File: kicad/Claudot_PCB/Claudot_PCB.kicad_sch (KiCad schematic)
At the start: 63 parts, among them J1 TYPE-C-31-M-12, J2 Conn_01x12, SW1 SW_Push, SW10 SW_Push, SW11 SW_Push, SW12 RotaryEncoder, SW2 SW_Push, SW3 SW_Push, SW4 SW_Push, SW5 SW_Push, SW6 SW_Push, SW7 SW_Push, SW8 SW_Push, SW9 SW_Push, U1 RP2040, U2 W25Q16JVUXIQ, U3 AP2112K-3.3, Y1 12MHz

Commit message: Update schematic and pcb
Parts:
- added J3: Conn_01x12, Library:AFC01-S12FCC-00, symbol Connector_Generic:Conn_01x12
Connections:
- net +3V3: now also J2.1 (Pin_1), J3.1 (Pin_1)
- net GND: now also J2.12 (Pin_12), J3.12 (Pin_12)
- net ROW1: now reaches SW7.1
- net ROW1: now also SW11.1, SW2.1, J3.3 (Pin_3)
- net COL0: now reaches D4.1 (K)
- net COL0: now also D1.1 (K), D2.1 (K), D3.1 (K), D5.1 (K), J3.7 (Pin_7)
- net ROW0: now reaches SW6.1
- net ROW0: now also SW1.1, SW10.1, J3.2 (Pin_2)
- net ROW3: now reaches SW4.1
- net ROW3: now also SW9.1, J3.5 (Pin_5)
- net ROW4: now reaches SW5.1
- net ROW4: now also J3.6 (Pin_6)
- net at U1.29 (GPIO18): now also J2.2 (Pin_2); no longer J2.1 (Pin_1)
- net at J2.10 (Pin_10): now also U1.38 (GPIO26_ADC0); no longer U1.39 (GPIO27_ADC1)
- net at J2.11 (Pin_11): now also U1.39 (GPIO27_ADC1); no longer U1.40 (GPIO28_ADC2)
- net at U1.41 (GPIO29_ADC3): no longer J2.12 (Pin_12)
- net at U1.30 (GPIO19): now also J2.3 (Pin_3); no longer J2.2 (Pin_2)
- net at U1.31 (GPIO20): now also J2.4 (Pin_4); no longer J2.3 (Pin_3)
- net at U1.32 (GPIO21): now also J2.5 (Pin_5); no longer J2.4 (Pin_4)
- net at U1.34 (GPIO22): now also J2.6 (Pin_6); no longer J2.5 (Pin_5)
- net at U1.35 (GPIO23): now also J2.7 (Pin_7); no longer J2.6 (Pin_6)
- net at U1.36 (GPIO24): now also J2.8 (Pin_8); no longer J2.7 (Pin_7)
- net at U1.37 (GPIO25): now also J2.9 (Pin_9); no longer J2.8 (Pin_8)
- net COL1: now reaches D7.1 (K)
- net COL1: now also D6.1 (K), D8.1 (K), D9.1 (K), J3.8 (Pin_8)
- net COL2: now reaches D11.1 (K)
- net COL2: now also D10.1 (K), J3.9 (Pin_9)
- net ROW2: now reaches SW8.1
- net ROW2: now also SW3.1, J3.4 (Pin_4)
- net IN-A renamed ROT1A
- net ROT1A: now also J3.10 (Pin_10)
- net IN-B renamed ROT1B
- net ROT1B: now also J3.11 (Pin_11)
- net SW12-A renamed SW12_A
- net SW12-B renamed SW12_B
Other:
- moved on the sheet: J2

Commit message: Update schematic and pcb
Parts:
- SW12: footprint Rotary_Encoder:RotaryEncoder_Alps_EC12E_Vertical_H20mm -> Library:EC12E
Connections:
- net +3V3: now also J3.12 (Pin_12); no longer J3.1 (Pin_1)
- net COL0: now also J3.6 (Pin_6); no longer J3.7 (Pin_7)
- net COL1: now also J3.5 (Pin_5); no longer J3.8 (Pin_8)
- net COL2: now also J3.4 (Pin_4); no longer J3.9 (Pin_9)
- net GND: now also J3.1 (Pin_1); no longer J3.12 (Pin_12)
- net ROT1A: now also J3.3 (Pin_3); no longer J3.10 (Pin_10)
- net ROT1B: now also J3.2 (Pin_2); no longer J3.11 (Pin_11)
- net ROW0: now also J3.11 (Pin_11); no longer J3.2 (Pin_2)
- net ROW1: now also J3.10 (Pin_10); no longer J3.3 (Pin_3)
- net ROW2: now also J3.9 (Pin_9); no longer J3.4 (Pin_4)
- net ROW3: now also J3.8 (Pin_8); no longer J3.5 (Pin_5)
- net ROW4: now also J3.7 (Pin_7); no longer J3.6 (Pin_6)
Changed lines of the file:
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@@
 	(symbol
 		(lib_id "Connector_Generic:Conn_01x12")
-		(at 104.14 96.52 0)
+		(at 104.14 99.06 0)
+		(mirror x)
 		(unit 1)
 		(exclude_from_sim no)
@@
 		(on_board yes)
 		(dnp no)
-		(fields_autoplaced yes)
 		(property "Reference" "J3"
 			(at 106.68 96.5199 0)
@@
 		)
 		(property "Footprint" "Library:AFC01-S12FCC-00"
-			(at 104.14 96.52 0)
+			(at 104.14 99.06 0)
 			(effects
 				(font
@@
 		)
 		(property "Datasheet" "~"
-			(at 104.14 96.52 0)
+			(at 104.14 99.06 0)
 			(effects
 				(font
@@
 		)
 		(property "Description" "Generic connector, single row, 01x12, script generated (kicad-library-utils/schlib/autogen/connector/)"
-			(at 104.14 96.52 0)
+			(at 104.14 99.06 0)
 			(effects
 				(font
@@
 			)
 		)
-		(property "Footprint" "Rotary_Encoder:RotaryEncoder_Alps_EC12E_Vertical_H20mm"
+		(property "Footprint" "Library:EC12E"
 			(at 104.14 58.166 0)
 			(effects

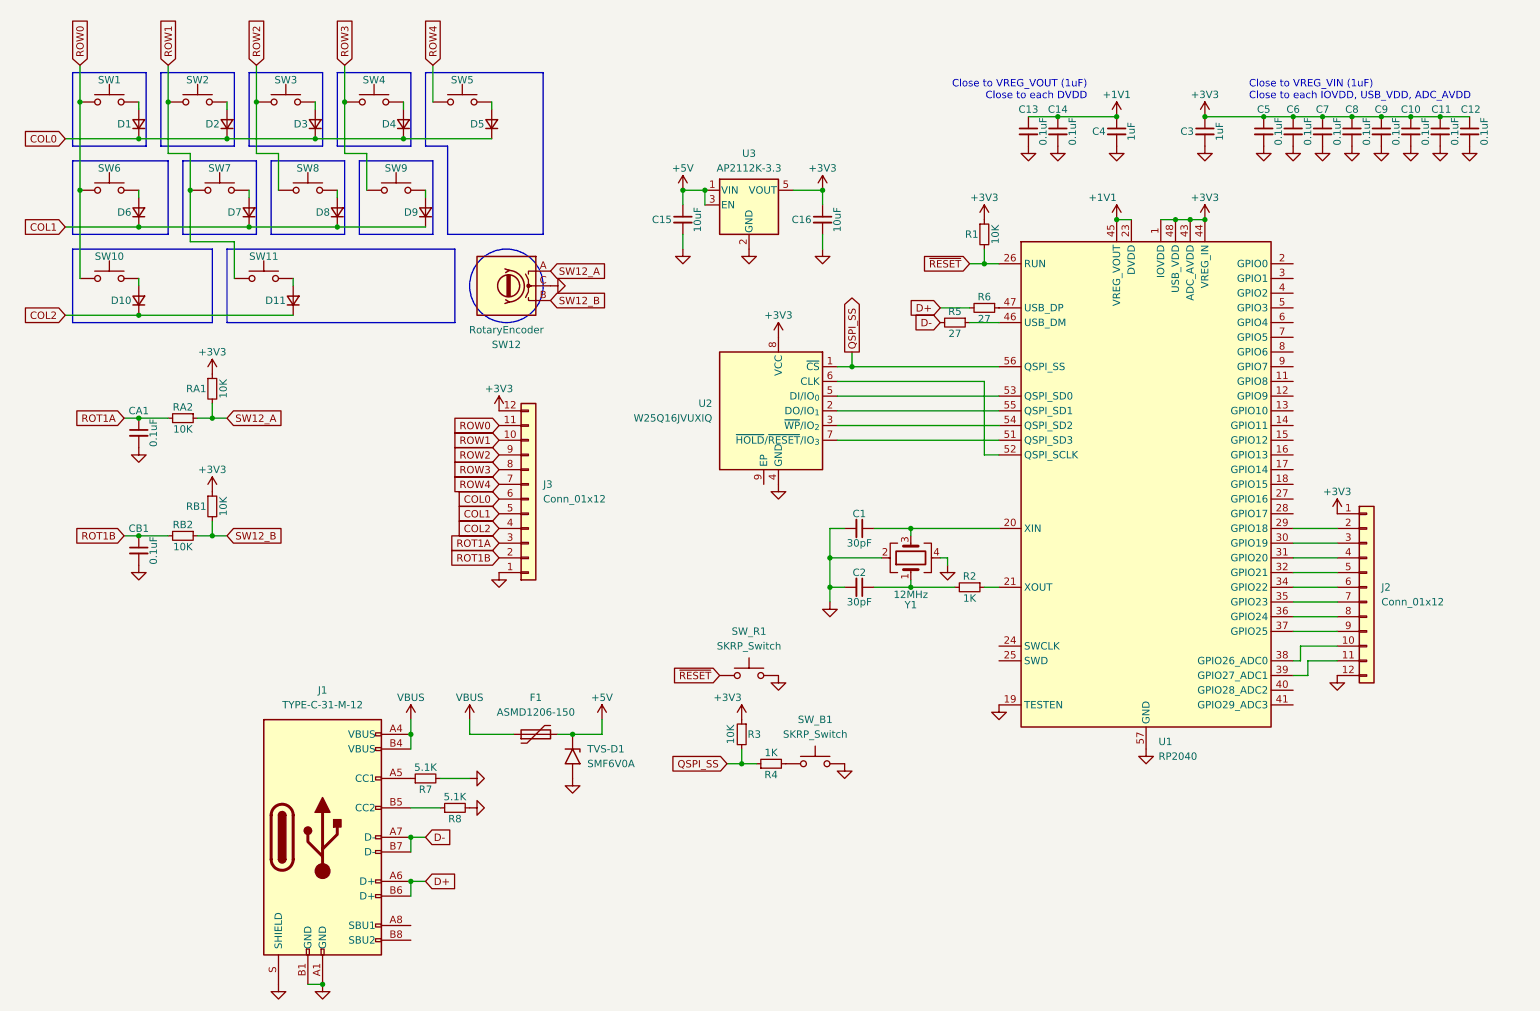
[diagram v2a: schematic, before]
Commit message: Separate PCB designs into individual KiCad projects
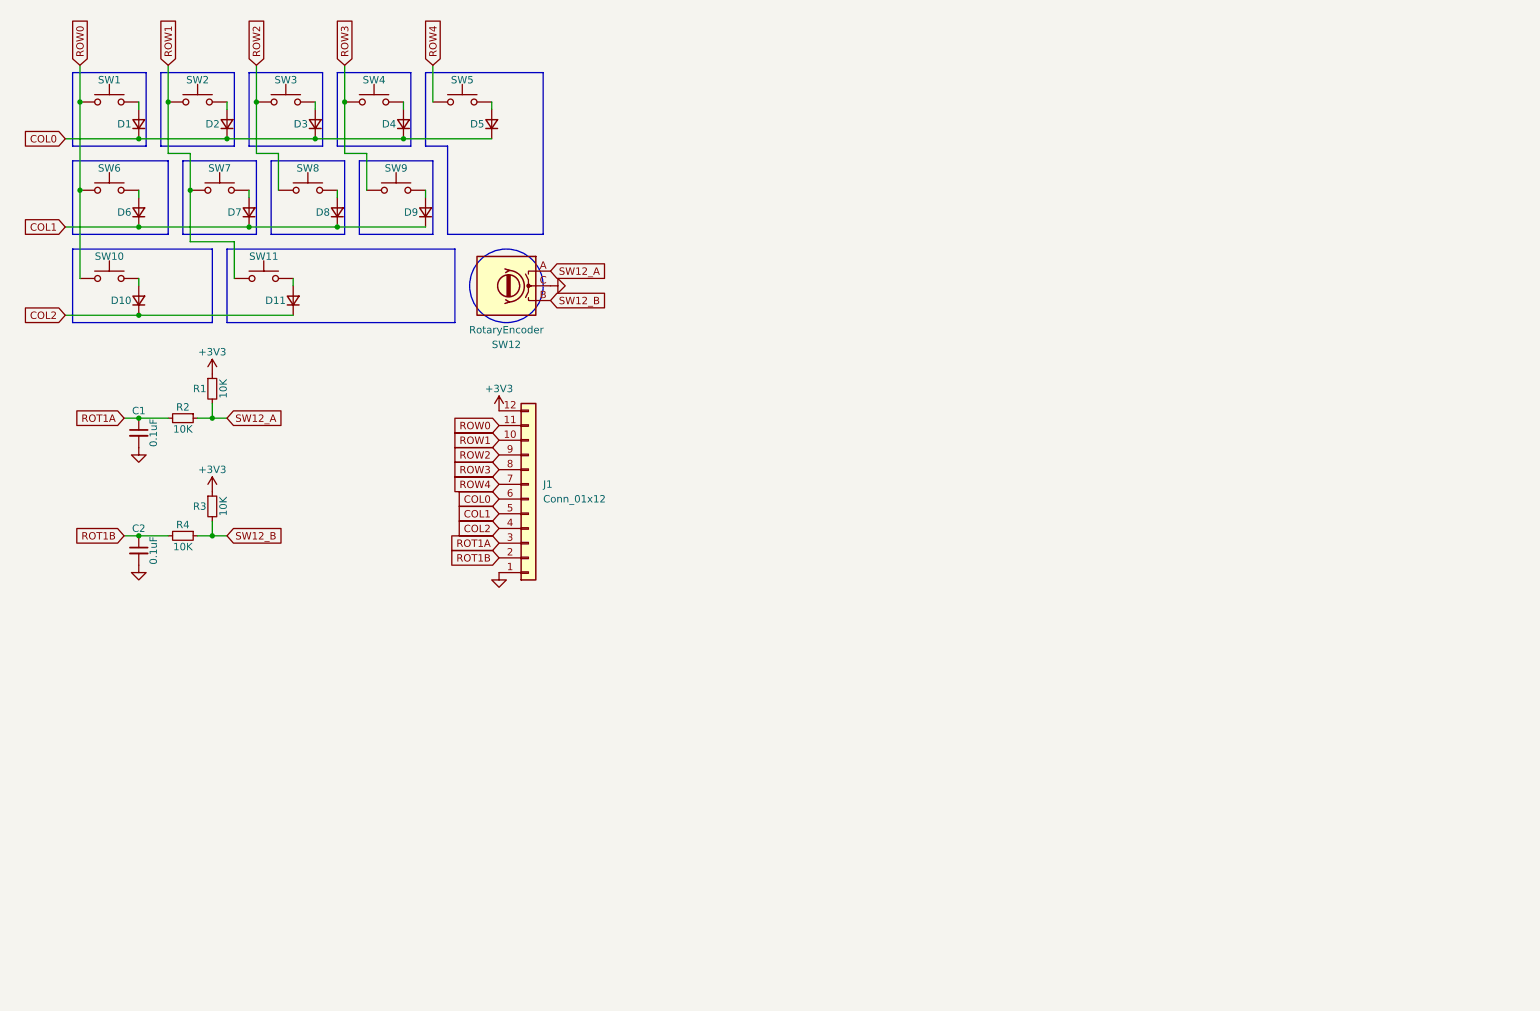
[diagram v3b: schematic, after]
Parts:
- removed C1, C2: 30pF, Library:C_0402, symbol Device:C_Small
- removed C10, C11, C12, C13, C14, C5, C6, C7, C8, C9: 0.1uF, Library:C_0402, symbol Device:C_Small
- removed C15, C16: 10uF, Library:C_0402, symbol Device:C_Small
- removed C3, C4: 1uF, Library:C_0402, symbol Device:C_Small
- removed F1: ASMD1206-150, Library:F_1206, symbol Device:Polyfuse
- removed J1: TYPE-C-31-M-12, Library:TYPE-C-31-M-12, symbol Library:TYPE-C-31-M-12
- removed J2: Conn_01x12, Library:AFC01-S12FCC-00, symbol Connector_Generic:Conn_01x12
- removed R1, R3: 10K, Library:R_0402, symbol Device:R_Small
- removed R2, R4: 1K, Library:R_0402, symbol Device:R_Small
- removed R5, R6: 27, Library:R_0402, symbol Device:R_Small
- removed R7, R8: 5.1K, Library:R_0402, symbol Device:R_Small
- removed SW_B1, SW_R1: SKRP_Switch, Library:SKRP_Switch, symbol Library:SKRP_Switch
- removed TVS-D1: SMF6V0A, Library:SMF6.0A, symbol Diode:SMF6V0A
- removed U1: RP2040, Library:RP2040, symbol MCU_RaspberryPi:RP2040
- removed U2: W25Q16JVUXIQ, Library:W25Q16JVUXIQ, symbol Library:W25Q16JVUXIQ
- removed U3: AP2112K-3.3, Library:SOT25, symbol Regulator_Linear:AP2112K-3.3
- removed Y1: 12MHz, Library:SMD3225-4P, symbol Device:Crystal_GND24
- renumbered CA1 to C1, CB1 to C2, J3 to J1, RA1 to R1, RA2 to R2, RB1 to R3, RB2 to R4
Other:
- note removed: "Close to VREG_VIN (1uF) Close to each IOVDD, USB_VDD, ADC_AVDD"
- note removed: "Close to VREG_VOUT (1uF) Close to each DVDD"

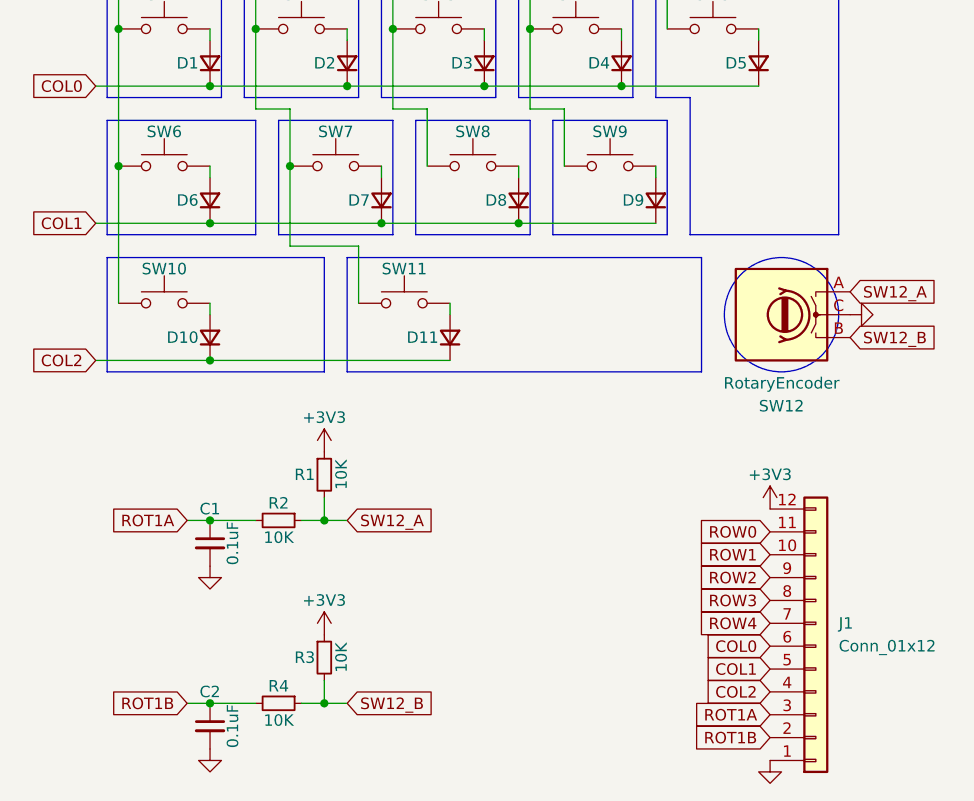
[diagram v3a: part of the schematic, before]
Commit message: kicad: replace rotary encoder with key
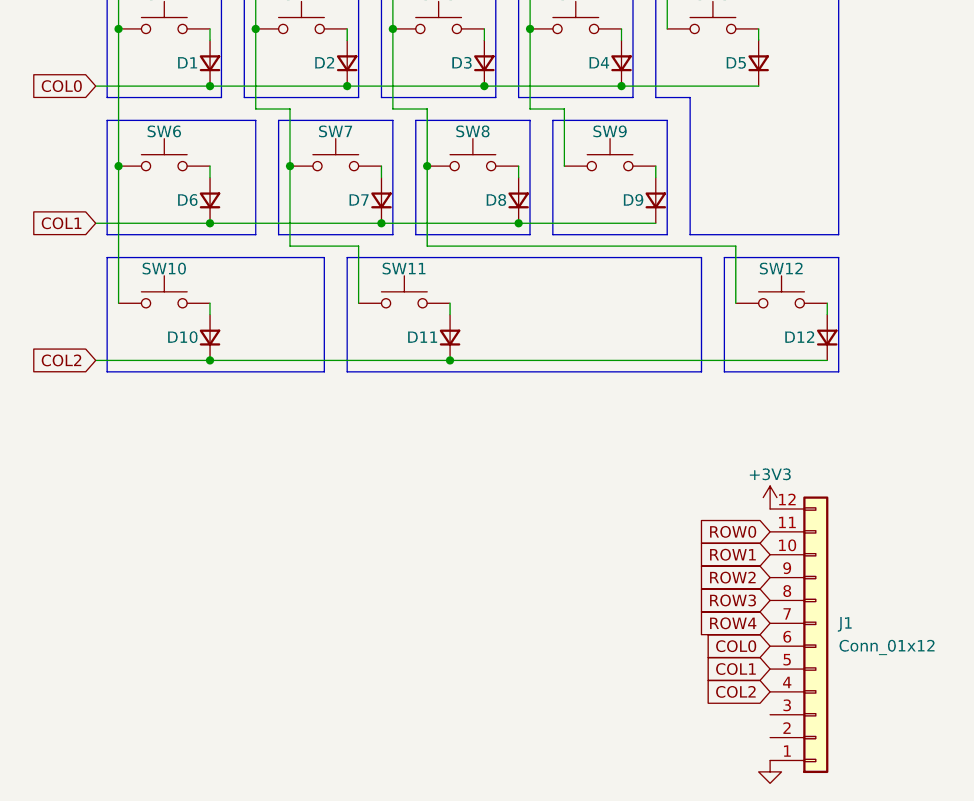
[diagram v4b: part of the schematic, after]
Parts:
- removed C1, C2: 0.1uF, Library:C_0402, symbol Device:C_Small
- removed R1, R2, R3, R4: 10K, Library:R_0402, symbol Device:R_Small
- removed SW12: RotaryEncoder, Library:EC12E, symbol Device:RotaryEncoder
- added D12: D_Small, Library:SOD323, symbol Device:D_Small
- added SW12: SW_Push, Library:CPG151101S11-16, symbol Switch:SW_Push
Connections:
- net COL2: now also D12.1 (K)
- net ROW2: now also SW12.1
- net ROT1A: no longer names the net of J1.3 (Pin_3)
- net ROT1B: no longer names the net of J1.2 (Pin_2)
- new net: D12.2 (A), SW12.2

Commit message: WIP
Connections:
- net +3V3: now also J1.2 (Pin_2); no longer J1.12 (Pin_12)
- net GND: now also J1.12 (Pin_12)

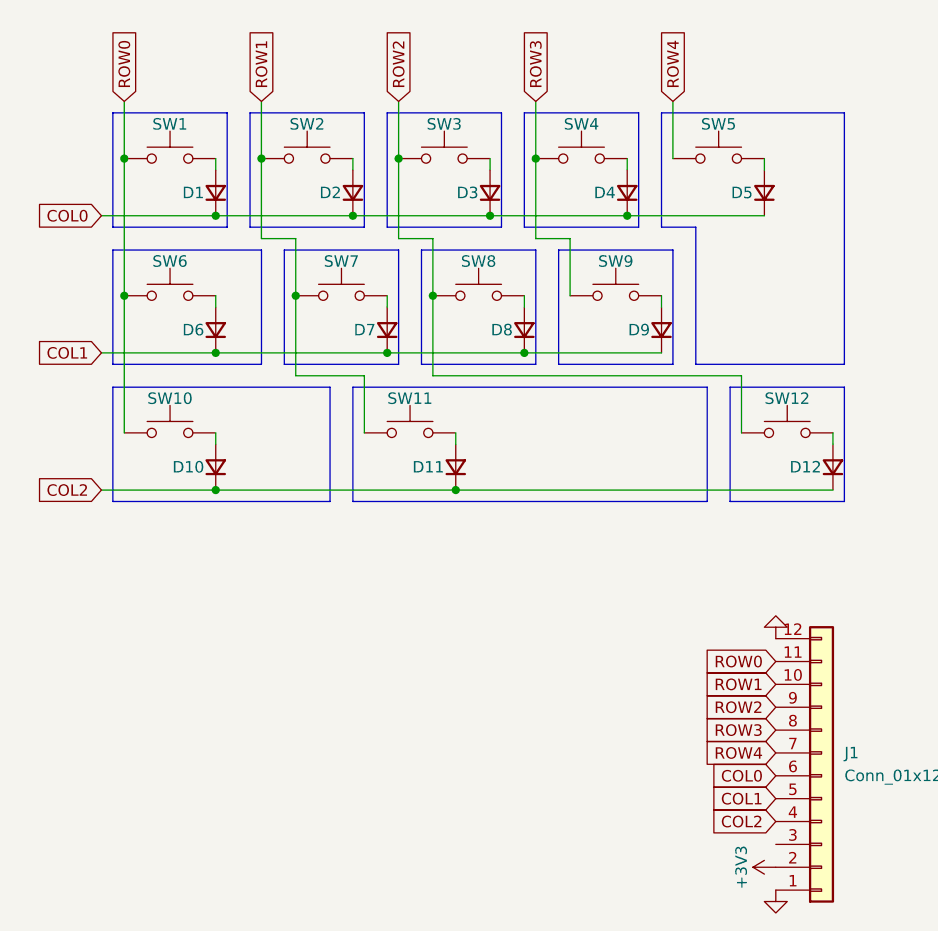
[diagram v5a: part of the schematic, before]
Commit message: fix: correct row/column net labels
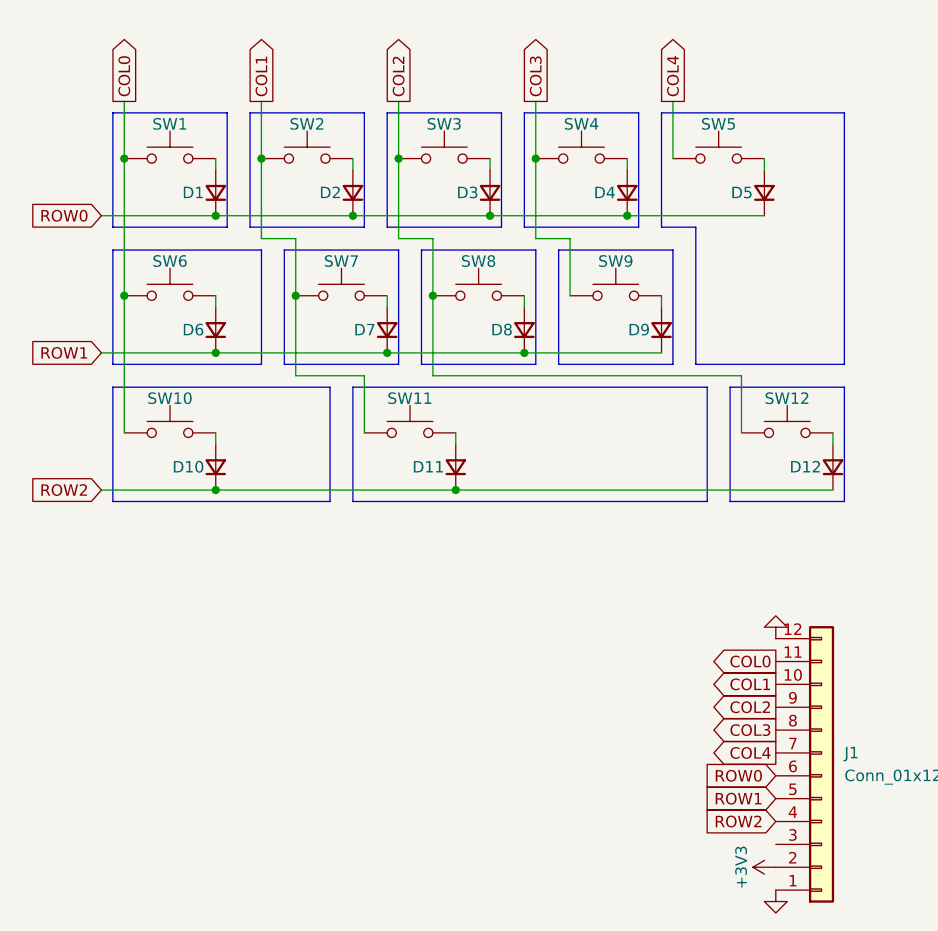
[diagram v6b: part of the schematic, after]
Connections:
- net COL0: now also J1.11 (Pin_11), SW1.1, SW10.1, SW6.1; no longer D1.1 (K), D2.1 (K), D3.1 (K), D4.1 (K), D5.1 (K), J1.6 (Pin_6)
- net COL1: now also J1.10 (Pin_10), SW11.1, SW2.1, SW7.1; no longer D6.1 (K), D7.1 (K), D8.1 (K), D9.1 (K), J1.5 (Pin_5)
- net COL2: now also J1.9 (Pin_9), SW12.1, SW3.1, SW8.1; no longer D10.1 (K), D11.1 (K), D12.1 (K), J1.4 (Pin_4)
- net ROW0: now also D1.1 (K), D2.1 (K), D3.1 (K), D4.1 (K), D5.1 (K), J1.6 (Pin_6); no longer J1.11 (Pin_11), SW1.1, SW10.1, SW6.1
- net ROW1: now also D6.1 (K), D7.1 (K), D8.1 (K), D9.1 (K), J1.5 (Pin_5); no longer J1.10 (Pin_10), SW11.1, SW2.1, SW7.1
- net ROW2: now also D10.1 (K), D11.1 (K), D12.1 (K), J1.4 (Pin_4); no longer J1.9 (Pin_9), SW12.1, SW3.1, SW8.1
- net ROW3 renamed COL3
- net ROW4 renamed COL4

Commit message: feat: finalize Claudot_PCB
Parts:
- removed J1: Conn_01x12, Library:AFC01-S12FCC-00, symbol Connector_Generic:Conn_01x12
- added J1: Conn_01x08, Library:AFC01-S08FCC-00, symbol Connector_Generic:Conn_01x08
- renumbered D11 to D10, D12 to D11, D5 to D12, D6 to D5, D7 to D6, D8 to D7, D9 to D8, D10 to D9, SW1 to KEY1, SW11 to KEY10, SW12 to KEY11, SW5 to KEY12, SW2 to KEY2, SW3 to KEY3, SW4 to KEY4, SW6 to KEY5, SW7 to KEY6, SW8 to KEY7, SW9 to KEY8, SW10 to KEY9
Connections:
- net COL4 is gone; now on net COL3: KEY12.1
- net COL0: now also J1.8 (Pin_8)
- net COL1: now also J1.7 (Pin_7)
- net COL2: now also J1.6 (Pin_6)
- net COL3: now also J1.5 (Pin_5)
- net GND: now also J1.1 (Pin_1)
- net ROW0: now also J1.3 (Pin_3); no longer D12.1 (K)
- net ROW1: now also J1.4 (Pin_4)
- net ROW2: now also D12.1 (K), J1.2 (Pin_2)

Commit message: chore: complete LCSC part numbers
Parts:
- D1, D10, D11, D12, D2, D3, D4, D5, D6, D7, D8, D9: value D_Small -> 1N4148WS; LCSC (none) -> C2128
- J1: LCSC (none) -> C262264
- KEY1, KEY10, KEY11, KEY12, KEY2, KEY3, KEY4, KEY5, KEY6, KEY7, KEY8, KEY9: LCSC (none) -> C41430893
